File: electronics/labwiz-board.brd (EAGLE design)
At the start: 98.8 x 51.3 mm, 133 parts, among them IC1 MCP3424, J1 SD_MICRO_SDIO_1BIT, J2 CORTEX_DEBUGSMD, J30 4P-SMD-2.0-90D, J4 4P-SMD-2.0-90D, J5 4P-SMD-2.0-90D, U1 STM32F10XRXT6, U4 MIC5219-3.3V, X2 M12_BOTTOM_CONTACTS_FPC_1MM, Y1 32.768kHz, Y3 32.768kHz

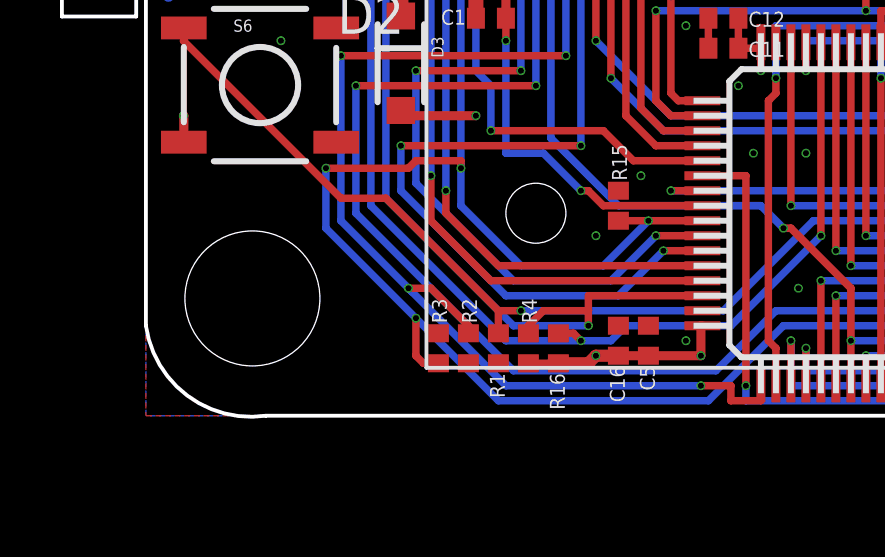
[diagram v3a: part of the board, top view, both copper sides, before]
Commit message: Added pullup to RESET.
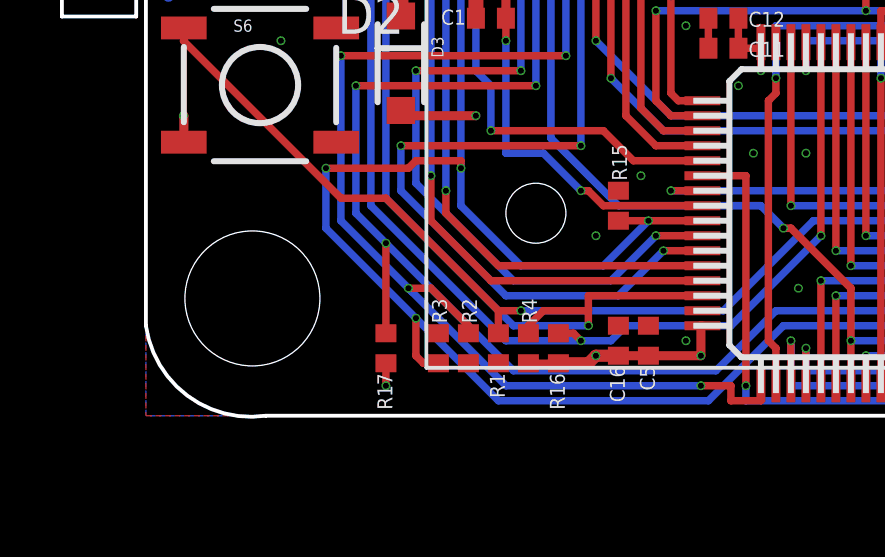
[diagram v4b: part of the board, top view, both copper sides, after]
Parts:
- added R17: 10K, PaxInstruments-RCL:0402
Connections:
- net 3.3V: now also R17.1
- net NRST: now also R17.2
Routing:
- net NRST: track 69.5 -> 72.5 mm, vias 4 -> 5
- net 3.3V: track 64.9 -> 65.6 mm, vias 27 -> 28
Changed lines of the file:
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@@
 <attribute name="POPULATE" value="" x="10.25" y="43.75" size="1" layer="27" display="off"/>
 </element>
+<element name="R17" library="PaxInstruments-RCL" package="0402" value="10K" x="8" y="2.25" rot="R90"/>
 </elements>
 <signals>
@@
 <wire x1="8.75" y1="45.5" x2="7.75" y2="45.5" width="0.25" layer="1"/>
 <wire x1="9.75" y1="43.75" x2="7.75" y2="43.75" width="0.25" layer="1"/>
+<contactref element="R17" pad="1"/>
+<via x="8" y="1" extent="1-16" drill="0.2"/>
+<wire x1="8" y1="1.75" x2="8" y2="1" width="0.25" layer="1"/>
 </signal>
 <signal name="GND" class="5">
@@
 <wire x1="21" y1="3.5" x2="19" y2="1.5" width="0.25" layer="16"/>
 <wire x1="19" y1="1.5" x2="12.25" y2="1.5" width="0.25" layer="16"/>
-<wire x1="12.25" y1="1.5" x2="7" y2="6.75" width="0.25" layer="16"/>
+<wire x1="12.25" y1="1.5" x2="8" y2="5.75" width="0.25" layer="16"/>
 <wire x1="12.5" y1="39.25" x2="12.25" y2="39.25" width="0.25" layer="1"/>
 <wire x1="12.25" y1="39.25" x2="11.75" y2="38.75" width="0.25" layer="1"/>
@@
 <wire x1="13" y1="36.25" x2="11.877" y2="36.25" width="0.25" layer="16"/>
 <wire x1="11.877" y1="36.25" x2="11.79" y2="36.337" width="0.25" layer="16"/>
+<contactref element="R17" pad="2"/>
+<wire x1="8" y1="2.75" x2="8" y2="5.75" width="0.25" layer="1"/>
+<via x="8" y="5.75" extent="1-16" drill="0.2"/>
+<wire x1="8" y1="5.75" x2="7" y2="6.75" width="0.25" layer="16"/>
 </signal>
 <signal name="OSC_IN">

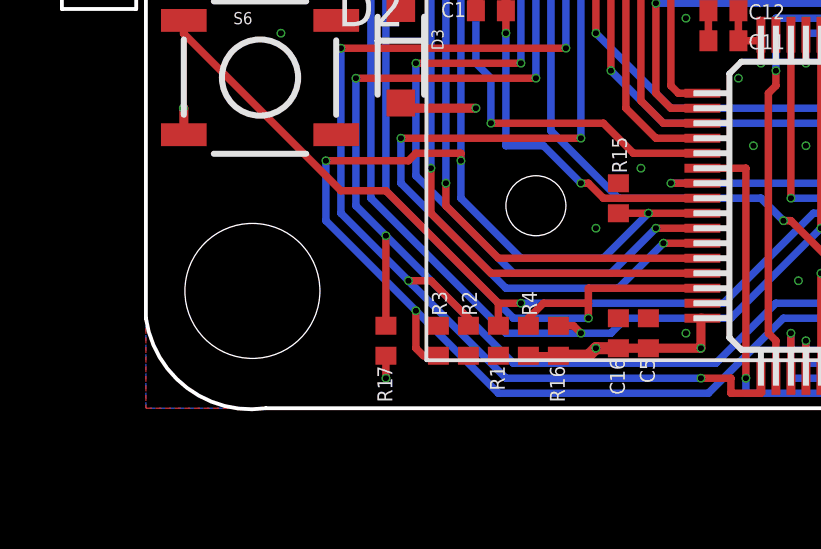
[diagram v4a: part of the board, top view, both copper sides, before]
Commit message: Added solder jumper for BOOT0. Closes #22.
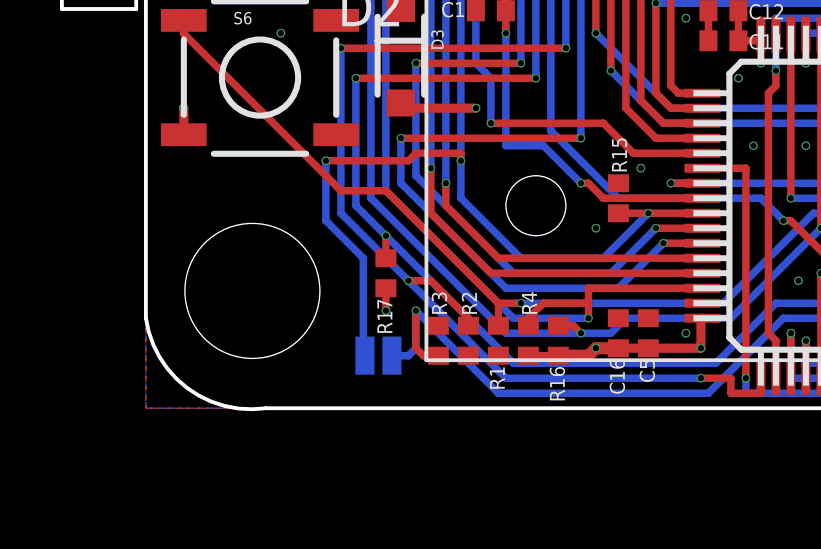
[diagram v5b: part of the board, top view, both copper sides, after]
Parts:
- added JP1: JUMPER-PAD-2-NOYES_SILK, SparkFun-Passives:PAD-JUMPER-2-NO_YES_SILK
- moved R17 2.25 mm to (8.00, 4.50)
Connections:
- new net N$69: JP1.2, R3.2, U1.60
- net SW_D_(BOOT0): now also JP1.1; no longer R3.2, U1.60
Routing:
- net N$69: track 0.00 -> 25.4 mm, vias 0 -> 2
- net SW_D_(BOOT0): track 81.9 -> 59.4 mm, vias 6 -> 4
- net NRST: track 72.5 -> 70.2 mm
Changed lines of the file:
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@@
 <attribute name="POPULATE" value="" x="10.25" y="43.75" size="1" layer="27" display="off"/>
 </element>
-<element name="R17" library="PaxInstruments-RCL" package="0402" value="10K" x="8" y="2.25" rot="R90"/>
+<element name="R17" library="PaxInstruments-RCL" package="0402" value="10K" x="8" y="4.5" rot="R90"/>
+<element name="JP1" library="SparkFun-Passives" package="PAD-JUMPER-2-NO_YES_SILK" value="JUMPER-PAD-2-NOYES_SILK" x="7.75" y="1.75" rot="MR180"/>
 </elements>
 <signals>
@@
 <wire x1="9.75" y1="43.75" x2="7.75" y2="43.75" width="0.25" layer="1"/>
 <contactref element="R17" pad="1"/>
-<via x="8" y="1" extent="1-16" drill="0.2"/>
-<wire x1="8" y1="1.75" x2="8" y2="1" width="0.25" layer="1"/>
+<via x="8" y="3.25" extent="1-16" drill="0.2"/>
+<wire x1="8" y1="4" x2="8" y2="3.25" width="0.25" layer="1"/>
 </signal>
 <signal name="GND" class="5">
@@
 <via x="3" y="38" extent="1-16" drill="0.2"/>
 <wire x1="1.25" y1="38" x2="1.264" y2="38" width="0.25" layer="1"/>
-<contactref element="U1" pad="60"/>
 <wire x1="1.5" y1="38" x2="3" y2="38" width="0.25" layer="1"/>
-<wire x1="26" y1="1.05" x2="26" y2="3" width="0.25" layer="1"/>
-<via x="26" y="3" extent="1-16" drill="0.2"/>
-<wire x1="26" y1="3" x2="21.25" y2="3" width="0.25" layer="16"/>
-<wire x1="21.25" y1="3" x2="18.75" y2="0.5" width="0.25" layer="16"/>
-<wire x1="18.75" y1="0.5" x2="11.75" y2="0.5" width="0.25" layer="16"/>
-<wire x1="11.75" y1="0.5" x2="9" y2="3.25" width="0.25" layer="16"/>
-<contactref element="R3" pad="2"/>
-<wire x1="9" y1="3.25" x2="6" y2="6.25" width="0.25" layer="16"/>
-<wire x1="9.75" y1="1.75" x2="9.25" y2="1.75" width="0.25" layer="1"/>
-<wire x1="9.25" y1="1.75" x2="9" y2="2" width="0.25" layer="1"/>
-<wire x1="9" y1="2" x2="9" y2="3.25" width="0.25" layer="1"/>
-<via x="9" y="3.25" extent="1-16" drill="0.2"/>
 <wire x1="6" y1="6.25" x2="6" y2="8.25" width="0.25" layer="16"/>
 <via x="6" y="8.25" extent="1-16" drill="0.2"/>
@@
 <via x="10.5" y="8.25" extent="1-16" drill="0.2"/>
 <wire x1="1.264" y1="38" x2="1.5" y2="38" width="0.4064" layer="1"/>
+<contactref element="JP1" pad="1"/>
+<wire x1="6" y1="6.25" x2="7.25" y2="5" width="0.25" layer="16"/>
+<wire x1="7.25" y1="5" x2="7.25" y2="1.8" width="0.25" layer="16"/>
+<wire x1="7.25" y1="1.8" x2="7.3" y2="1.75" width="0.25" layer="16"/>
 </signal>
 <signal name="SW_B">
@@
 <wire x1="11.877" y1="36.25" x2="11.79" y2="36.337" width="0.25" layer="16"/>
 <contactref element="R17" pad="2"/>
-<wire x1="8" y1="2.75" x2="8" y2="5.75" width="0.25" layer="1"/>
+<wire x1="8" y1="5" x2="8" y2="5.75" width="0.25" layer="1"/>
 <via x="8" y="5.75" extent="1-16" drill="0.2"/>
 <wire x1="8" y1="5.75" x2="7" y2="6.75" width="0.25" layer="16"/>
@@
 <via x="75" y="46" extent="1-16" drill="0.6" shape="square"/>
 </signal>
+<signal name="N$69">
+<contactref element="U1" pad="60"/>
+<contactref element="R3" pad="2"/>
+<wire x1="26" y1="1.05" x2="26" y2="3" width="0.25" layer="1"/>
+<via x="26" y="3" extent="1-16" drill="0.2"/>
+<wire x1="26" y1="3" x2="21.25" y2="3" width="0.25" layer="16"/>
+<wire x1="21.25" y1="3" x2="18.75" y2="0.5" width="0.25" layer="16"/>
+<wire x1="18.75" y1="0.5" x2="11.75" y2="0.5" width="0.25" layer="16"/>
+<wire x1="11.75" y1="0.5" x2="9" y2="3.25" width="0.25" layer="16"/>
+<wire x1="9.75" y1="1.75" x2="9.25" y2="1.75" width="0.25" layer="1"/>
+<wire x1="9.25" y1="1.75" x2="9" y2="2" width="0.25" layer="1"/>
+<wire x1="9" y1="2" x2="9" y2="3.25" width="0.25" layer="1"/>
+<via x="9" y="3.25" extent="1-16" drill="0.2"/>
+<contactref element="JP1" pad="2"/>
+<wire x1="8.2" y1="1.75" x2="8.75" y2="1.75" width="0.25" layer="16"/>
+<wire x1="8.75" y1="1.75" x2="9" y2="2" width="0.25" layer="16"/>
+<wire x1="9" y1="2" x2="9" y2="3.25" width="0.25" layer="16"/>
+</signal>
 </signals>

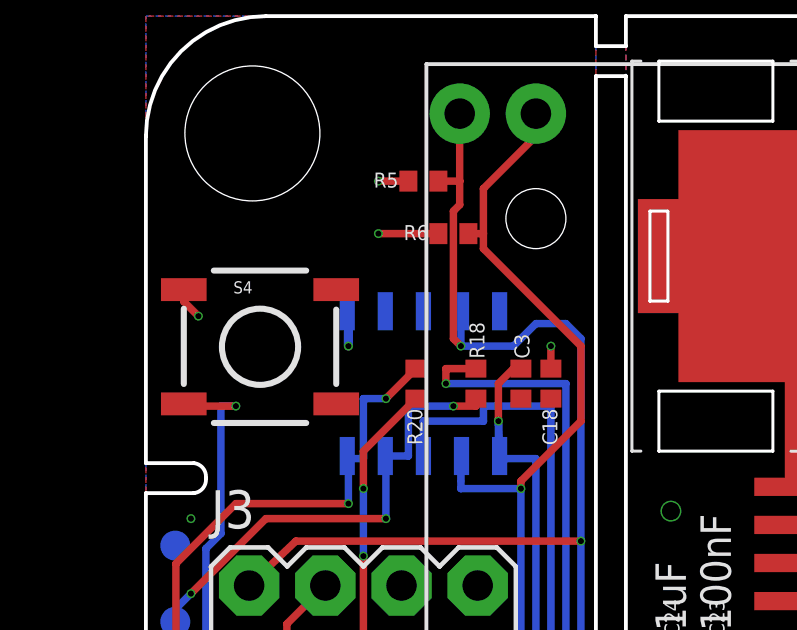
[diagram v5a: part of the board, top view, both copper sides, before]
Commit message: Added RESET switch.
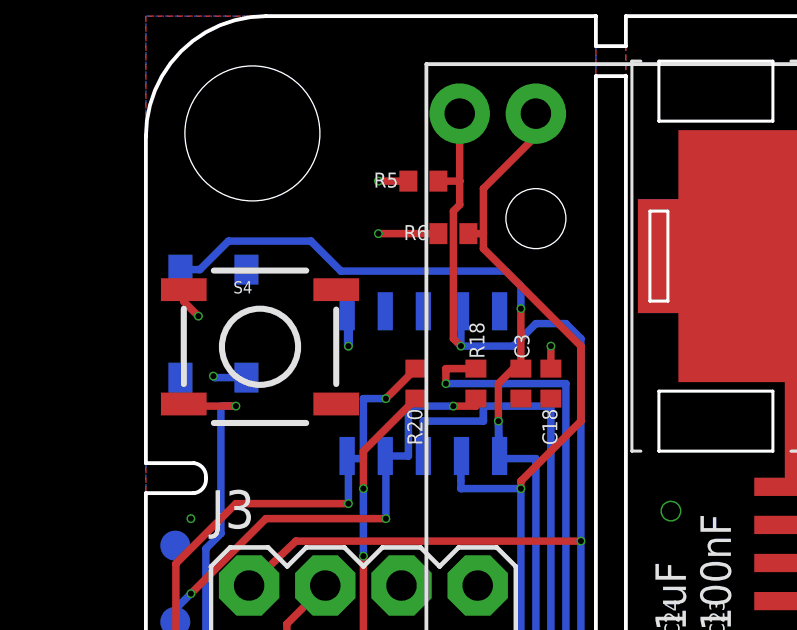
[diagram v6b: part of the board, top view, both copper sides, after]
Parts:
- added S7: SWITCH-MOMENTARY-2SMD-3, PaxInstruments-Electromechanical:TACTILE_SWITCH_SMD-3
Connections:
- net GND: now also S7.1
- net NRST: now also S7.4
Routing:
- net NRST: track 70.2 -> 85.3 mm, vias 5 -> 6
- net GND: track 25.6 -> 26.7 mm, vias 76 -> 77
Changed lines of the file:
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@@
 <element name="R17" library="PaxInstruments-RCL" package="0402" value="10K" x="8" y="4.5" rot="R90"/>
 <element name="JP1" library="SparkFun-Passives" package="PAD-JUMPER-2-NO_YES_SILK" value="JUMPER-PAD-2-NOYES_SILK" x="7.75" y="1.75" rot="MR180"/>
+<element name="S7" library="PaxInstruments-Electromechanical" package="TACTILE_SWITCH_SMD-3" value="SWITCH-MOMENTARY-2SMD-3" x="2.25" y="40.75" rot="MR90"/>
 </elements>
 <signals>
@@
 <via x="16.5" y="8" extent="1-16" drill="0.2"/>
 <via x="1.5" y="34.25" extent="1-16" drill="0.2"/>
+<contactref element="S7" pad="1"/>
+<via x="2.25" y="39" extent="1-16" drill="0.2"/>
+<wire x1="3.35" y1="38.95" x2="2.3" y2="38.95" width="0.25" layer="16"/>
+<wire x1="2.3" y1="38.95" x2="2.25" y2="39" width="0.25" layer="16"/>
 </signal>
 <signal name="N$3">
@@
 <via x="8" y="5.75" extent="1-16" drill="0.2"/>
 <wire x1="8" y1="5.75" x2="7" y2="6.75" width="0.25" layer="16"/>
+<contactref element="S7" pad="4"/>
+<wire x1="1.15" y1="42.55" x2="1.8" y2="42.55" width="0.25" layer="16"/>
+<wire x1="1.8" y1="42.55" x2="2.75" y2="43.5" width="0.25" layer="16"/>
+<wire x1="2.75" y1="43.5" x2="5.5" y2="43.5" width="0.25" layer="16"/>
+<wire x1="5.5" y1="43.5" x2="6.5" y2="42.5" width="0.25" layer="16"/>
+<wire x1="6.5" y1="42.5" x2="12" y2="42.5" width="0.25" layer="16"/>
+<wire x1="12" y1="42.5" x2="12.5" y2="42" width="0.25" layer="16"/>
+<wire x1="12.5" y1="42" x2="12.5" y2="41.25" width="0.25" layer="16"/>
+<via x="12.5" y="41.25" extent="1-16" drill="0.2"/>
+<wire x1="12.5" y1="41.25" x2="12.5" y2="39.25" width="0.25" layer="1"/>
 </signal>
 <signal name="OSC_IN">
